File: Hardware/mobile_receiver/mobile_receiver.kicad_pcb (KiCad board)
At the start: 4 copper layers, 82.5 x 142 mm, 32 parts, among them J1 Conn_02x07_Top_Bottom, SW1 SW_SPST, SW2 SW_Push, SW3 SW_Push, SW4 SW_Push, SW5 SW_Push, SW6 SW_Push, SW7 SW_Push, U2 kb2040

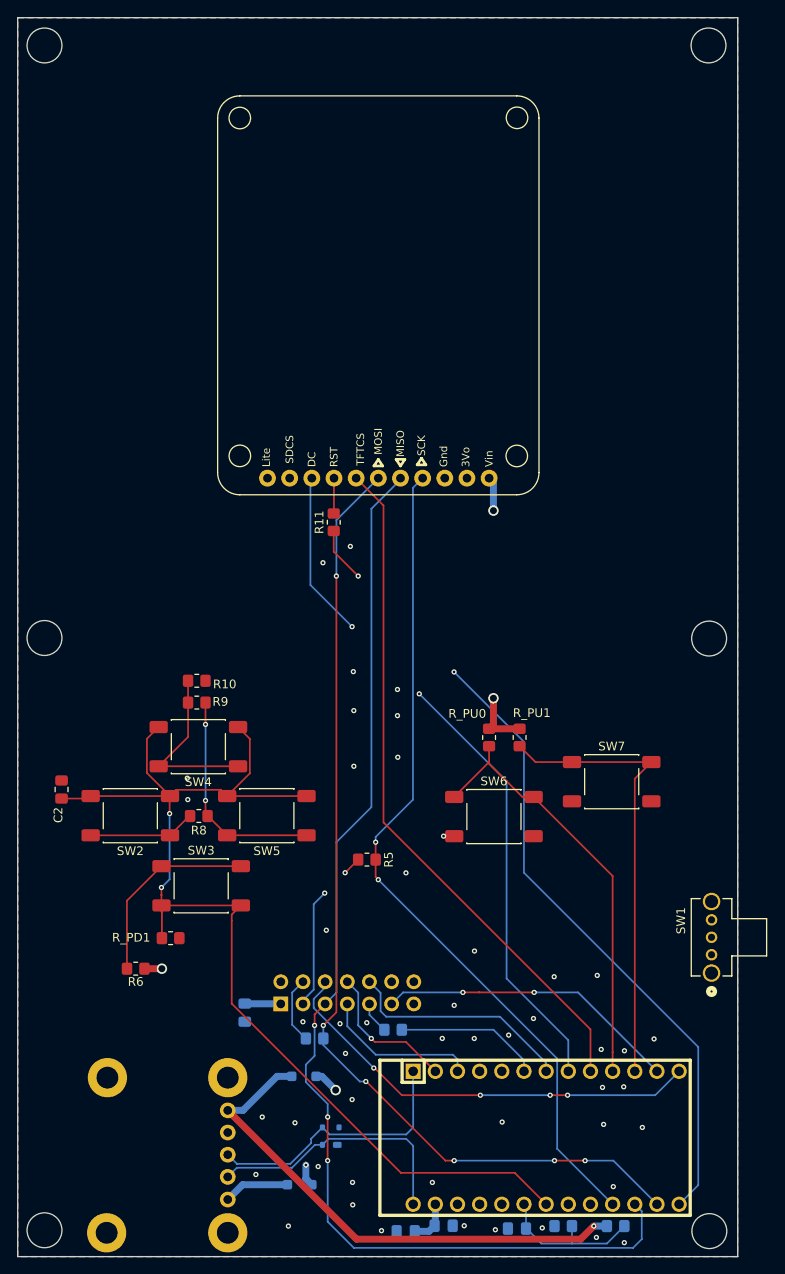
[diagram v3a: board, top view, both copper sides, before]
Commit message: Fixed RF trace, Added new Diodes, better power traces and new switches
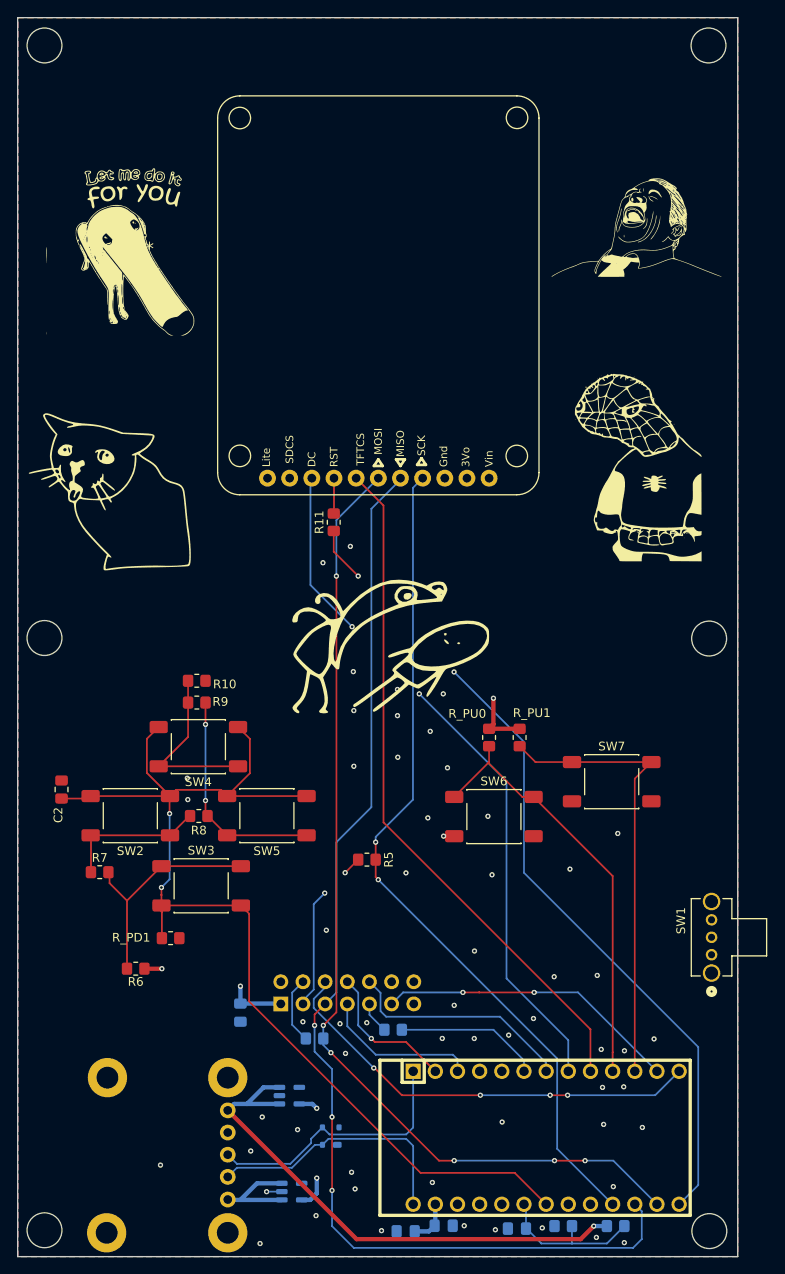
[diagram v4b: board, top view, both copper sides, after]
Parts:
- removed D1, D2: DS, Diode_SMD:D_SOD-123F
- added G***: LOGO, footprints:spooderman, F.Cu at (237.5, 131.5)
- added G***: LOGO, footprints:cat2, F.Cu at (177.2, 134.5)
- added G***: LOGO, footprints:shouting, F.Cu at (205.5, 153.0)
- added G***: LOGO, footprints:laughing, F.Cu at (237.5, 104.0)
- added G***: LOGO, My footprints:letmedoitforyou, F.Cu at (179.8, 106.5)
- added G***: LOGO, footprints:onepiece, B.Cu at (209.2, 118.2)
- added R7: 10K, Resistor_SMD:R_0805_2012Metric_Pad1.20x1.40mm_HandSolder, F.Cu at (175.9, 177.9)
- added U4: MAX40200AUK, Package_TO_SOT_SMD:SOT-23-5, B.Cu at (197.9, 214.6)
- added U6: MAX40200AUK, Package_TO_SOT_SMD:SOT-23-5, B.Cu at (197.6, 203.6)
- moved C3 0.50 mm to (192.0, 194.0)
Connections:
- SW1 pad 2: Net-(D1-K) -> /SUMMED_POWER
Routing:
- net /SUMMED_POWER: track 0.00 -> 67.4 mm, vias 0 -> 2
- net Net-(D1-K): track 65.8 -> 0.00 mm, vias 2 -> 0
- net Net-(R7-Pad1): track 12.3 -> 16.6 mm
- net /USB_5V: track 7.54 -> 11.8 mm
- net Net-(R6-Pad1): track 22.5 -> 26.5 mm
- net /DPAD_ADC: track 131.5 -> 129.3 mm
- net /VBAT: track 59.1 -> 60.9 mm
- net GND: track 0.00 -> 1.75 mm, vias 49 -> 58
- net +3.3V: track 148.5 -> 147.2 mm
- net /SYS_MISO: track 132.7 -> 131.9 mm
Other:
- board text added: "3Vo"
- board text added: "Gnd"
- board text added: "MISO"
- board text added: "MOSI"
- board text added: "RST"
- board text added: "SCK"
- board text added: "TFTCS"
- board text added: "Vin"

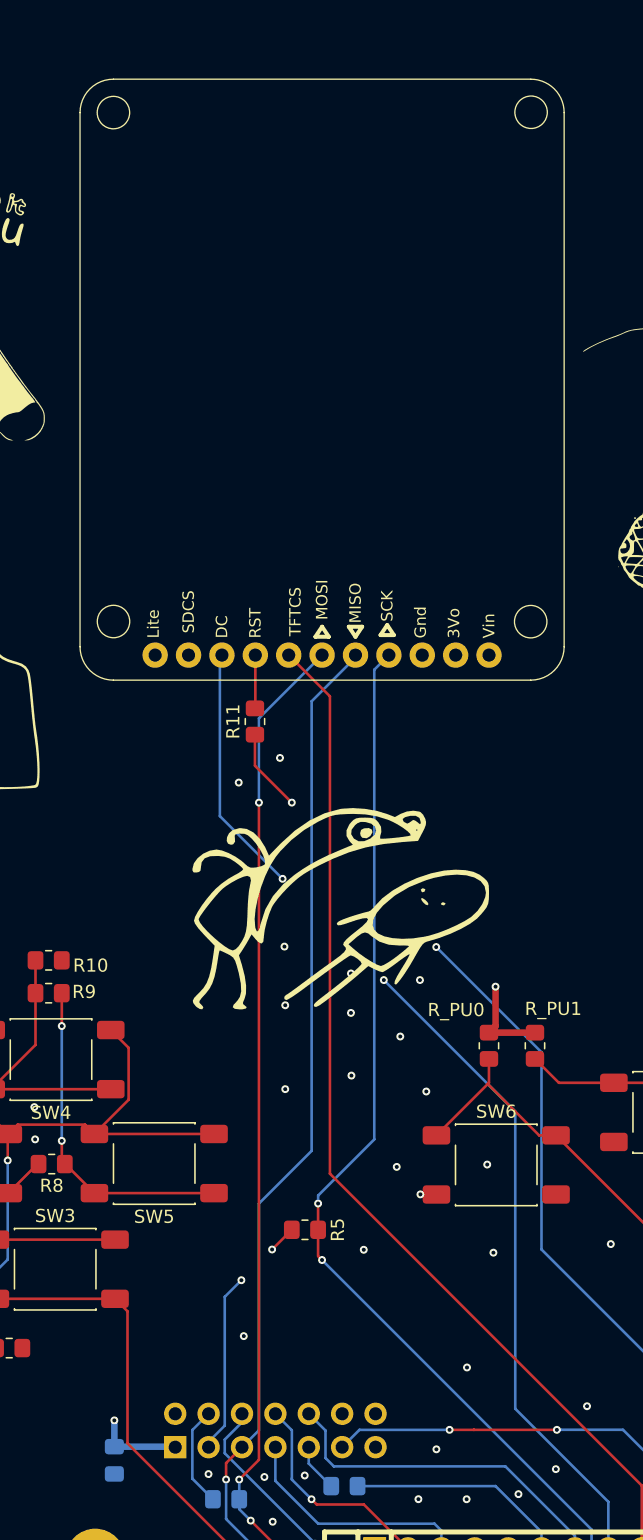
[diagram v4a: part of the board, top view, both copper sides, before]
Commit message: adding fixed screen
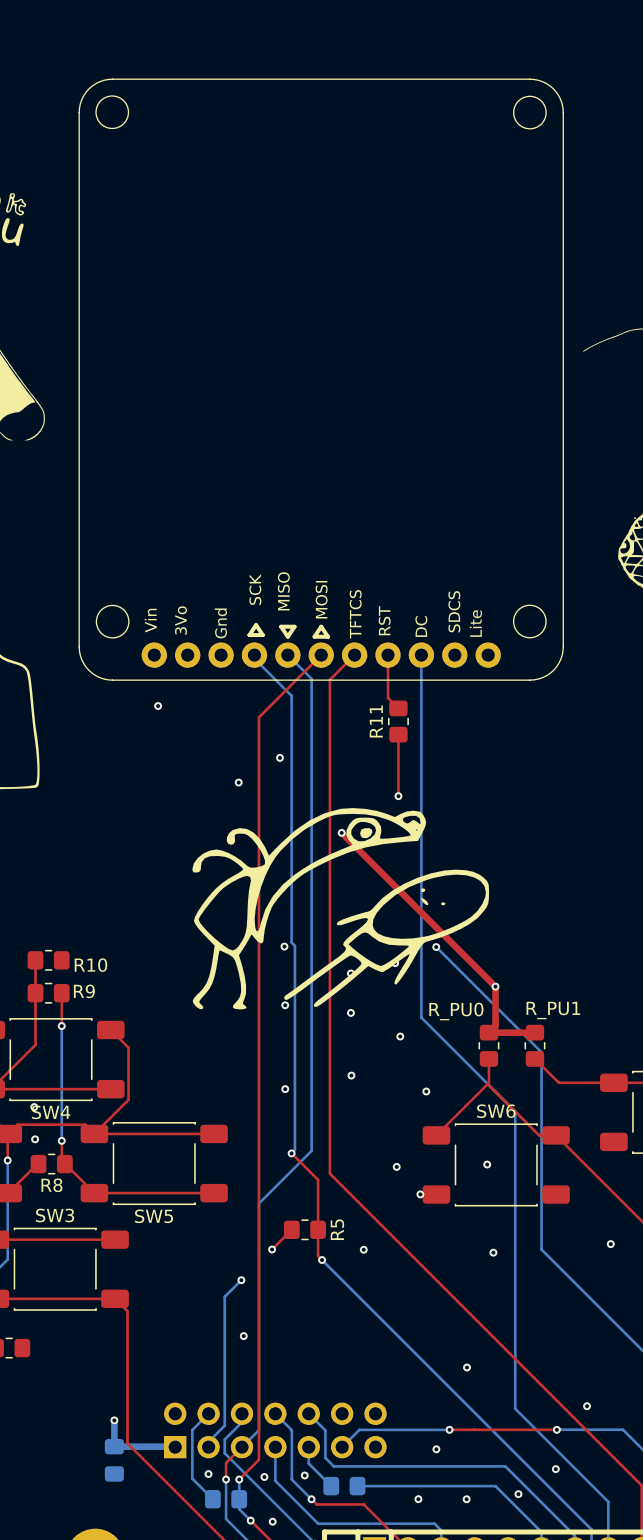
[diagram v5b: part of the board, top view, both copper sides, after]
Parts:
- moved R11 10.9 mm to (213.6, 137.8)
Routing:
- net +3.3V: track 147.2 -> 157.8 mm, vias 3 -> 4
- net /TFT_DC: track 80.3 -> 73.9 mm, vias 2 -> 0
- net /TFT_RESET: track 95.4 -> 90.9 mm
- net unconnected-(U3-LITE-Pad11): track 0.00 -> 1.40 mm
- net /SYS_MISO: track 131.9 -> 131.3 mm
- net GND: track 1.75 -> 1.98 mm, vias 58 -> 59
- net /SYS_MOSI: vias 6 -> 5

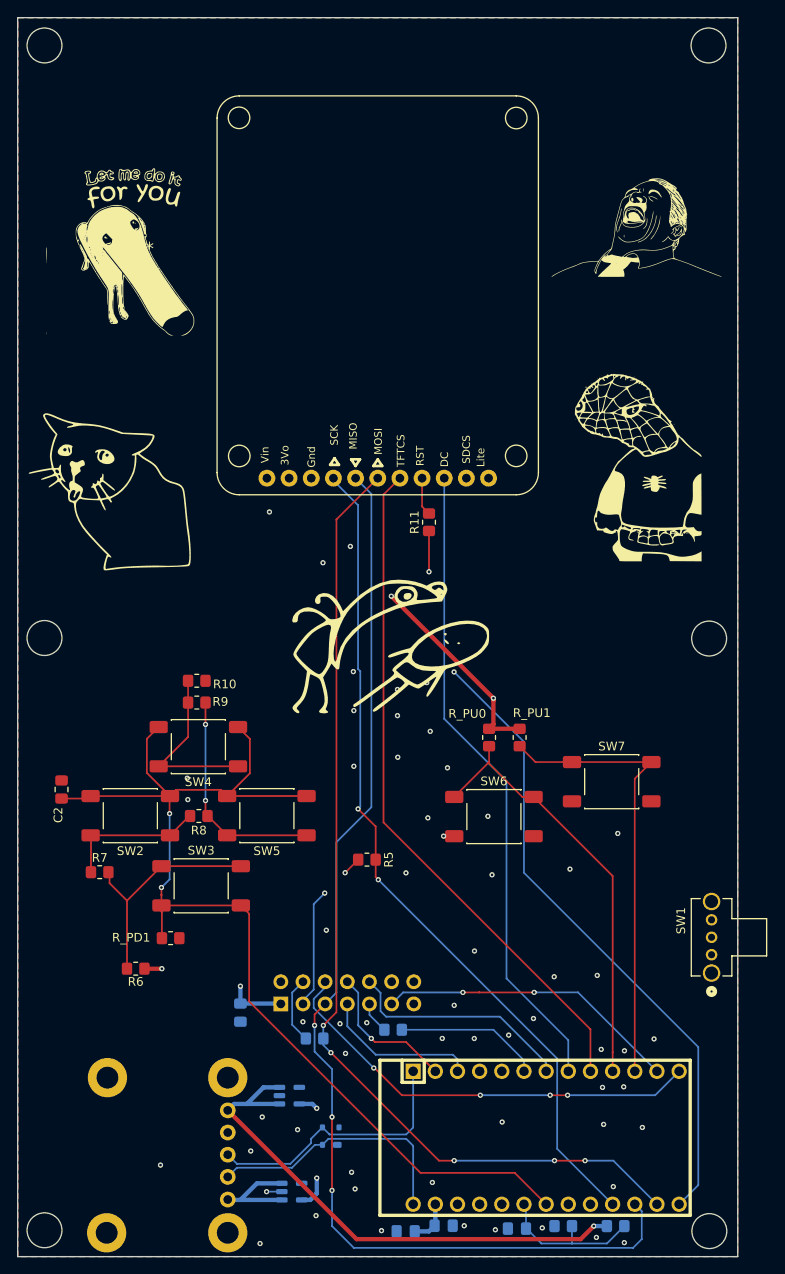
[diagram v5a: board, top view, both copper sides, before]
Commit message: Added HiPR logos and fixed mounting wholes
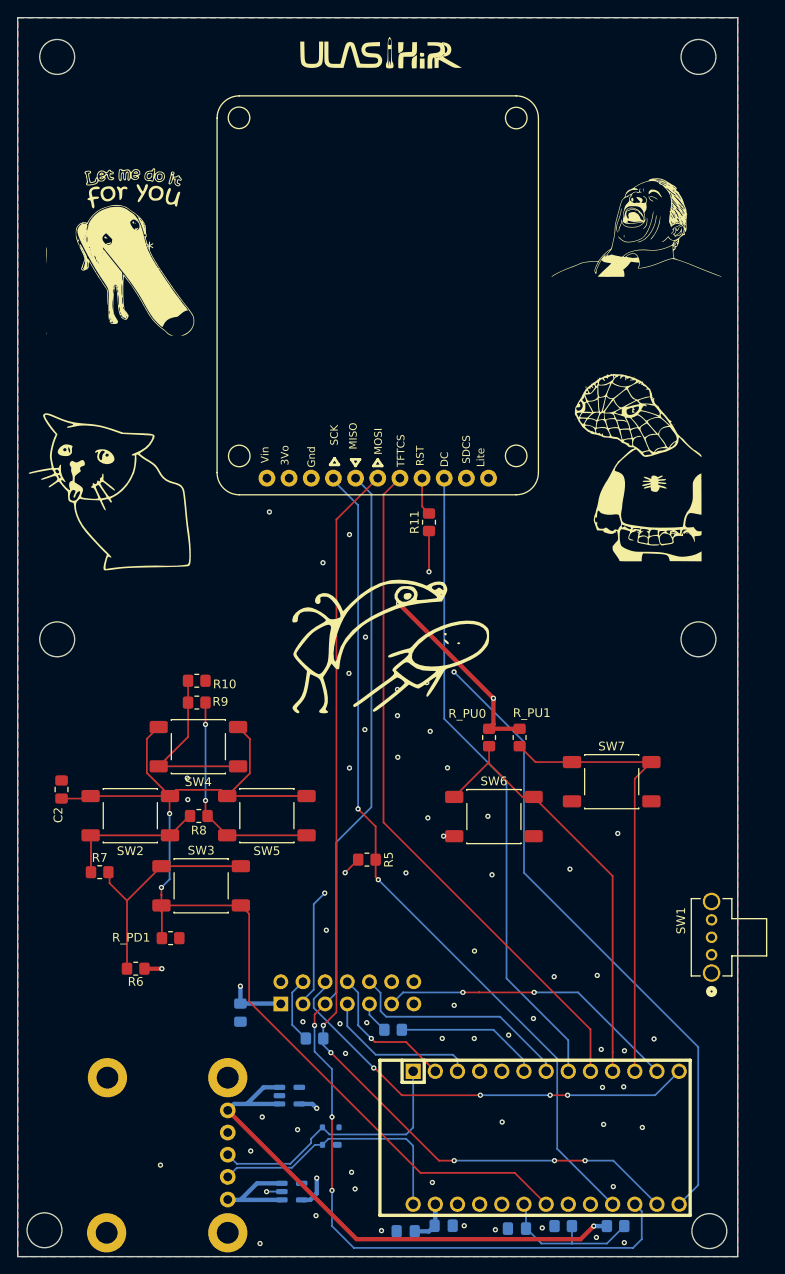
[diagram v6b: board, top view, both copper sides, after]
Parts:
- added G***: LOGO, footprints:HiPR, F.Cu at (208.0, 84.2)
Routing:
- net +3.3V: track 157.8 -> 158.5 mm
- net GND: vias 59 -> 60
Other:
- outline, holes or cut-outs redrawn

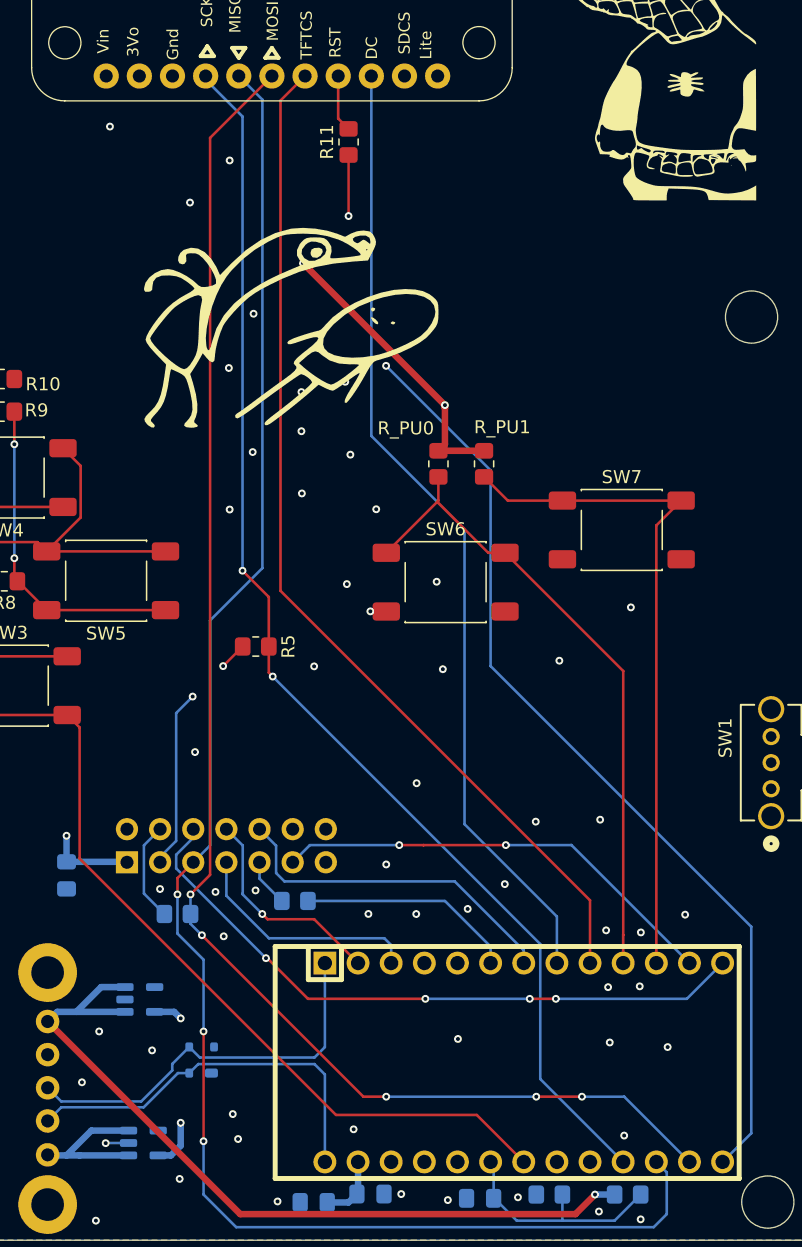
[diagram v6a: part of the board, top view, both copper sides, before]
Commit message: SPI resistors removed and transmission added
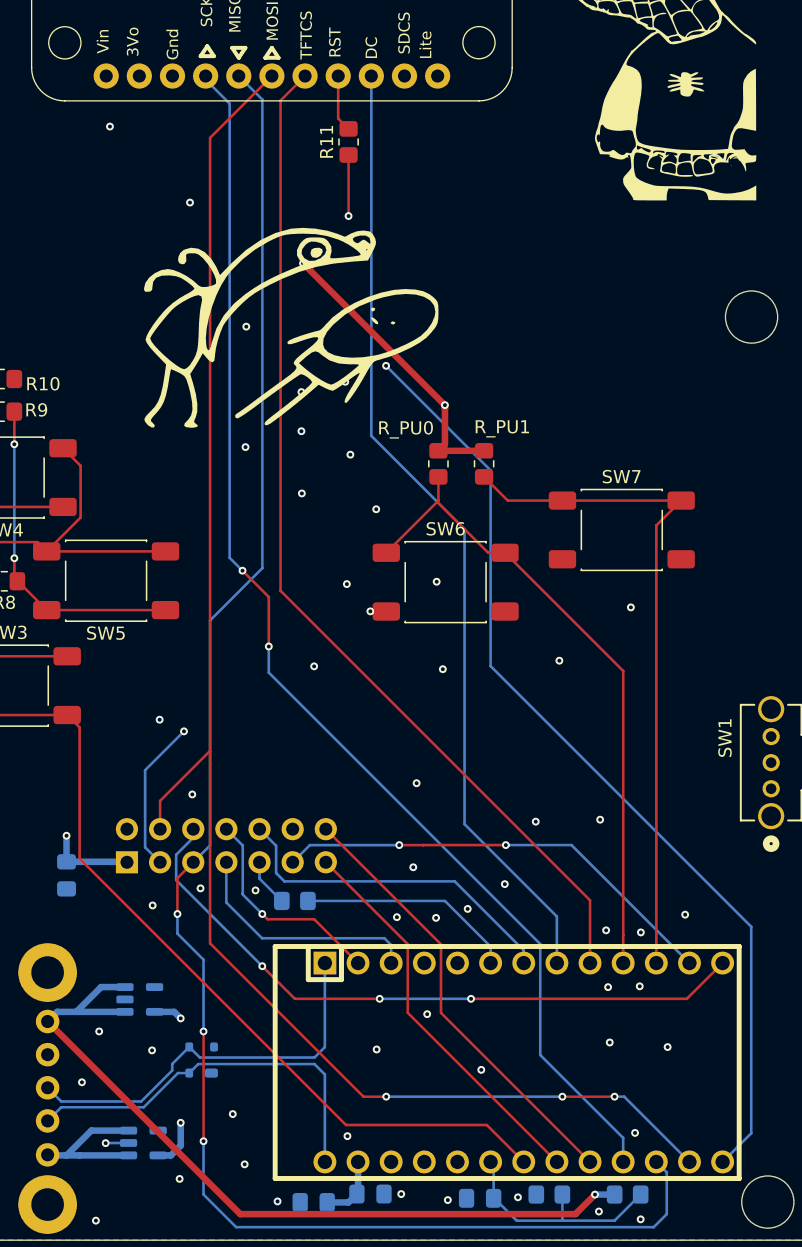
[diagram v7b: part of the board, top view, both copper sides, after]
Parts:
- removed R4, R5: 10K, Resistor_SMD:R_0805_2012Metric_Pad1.20x1.40mm_HandSolder
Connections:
- J1 pad 13: /GPIO1 -> /TX_SWITCH
- J1 pad 14: /GPIO2 -> /RX_SWITCH
- J1 pad 3: Net-(J1-Pin_3) -> /SYS_SCK
- J1 pad 4: Net-(J1-Pin_4) -> /SYS_MOSI
- U2 pad 21: unconnected-(U2-A1/27-Pad21) -> /TX_SWITCH
- U2 pad 22: unconnected-(U2-A0/26-Pad22) -> /RX_SWITCH
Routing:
- net /RX_SWITCH: track 0.00 -> 33.9 mm
- net /TX_SWITCH: track 0.00 -> 30.3 mm
- net /SYS_SCK: track 96.5 -> 117.8 mm, vias 2 -> 3
- net Net-(J1-Pin_3): track 19.2 -> 0.00 mm, vias 2 -> 0
- net Net-(J1-Pin_4): track 7.67 -> 0.00 mm
- net /SYS_MOSI: track 113.4 -> 119.7 mm, vias 5 -> 3
- net /SPI_CS: track 50.7 -> 51.2 mm, vias 4 -> 3
- net GND: vias 60 -> 59

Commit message: hardware done
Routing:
- added copper zone on In2.Cu, net GND
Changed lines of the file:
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@@
 			(drillshape 0)
 			(scaleselection 1)
-			(outputdirectory "../Manufacturing/mobile_receiver/Drill Files/")
+			(outputdirectory "../Manufacturing/mobile_receiver/fabrication/")
 		)
 	)
@@
 		(net 1)
 		(net_name "GND")
-		(layers "F.Cu" "B.Cu")
+		(layers "F.Cu" "B.Cu" "In1.Cu" "In2.Cu")
 		(hatch edge 0.5)
 		(priority 1)
